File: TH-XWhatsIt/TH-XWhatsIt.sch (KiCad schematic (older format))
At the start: 33 parts, among them J1 COLUMNS, J12 EXPANSION HEADER, J2 ROWS, U1 LM339, U2 MCP4921-EP, U3 74HCT595, U5 74HCT595, U6 LM339, U7 ProMicro, U8 74HCT595

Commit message: Added pads to short reset on bottom
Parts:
- added J13: Conn_01x02, TH-XWhatsIt:PadsToShort, symbol Connector_Generic:Conn_01x02
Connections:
- net GNDA: now also J13.1 (Pin_1)
- net RESET: now reaches U7.22 (RST)
- net RESET: now also J13.2 (Pin_2)
- no-connect marks 5 -> 4
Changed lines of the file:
@@
 $EndComp
 NoConn ~ 9850 2725
-NoConn ~ 9850 2925
 Text GLabel 8450 3225 0    50   Input ~ 0
 ROW1
@@
 ROW7
 Wire Wire Line
-	2000 2075 1775 2075
-Wire Wire Line
 	1625 2075 1625 1475
 Connection ~ 1625 1475
@@
 	1    0    0    -1
 $EndComp
-Connection ~ 1775 2075
-Wire Wire Line
-	1775 2075 1725 2075
 Connection ~ 1725 2075
 Wire Wire Line
@@
 Text Notes 1025 750  0    50   ~ 0
 Either mount just the resistor networks,\nor mount just the individual pulls to BIAS.
+Wire Wire Line
+	1725 2075 2000 2075
+Text GLabel 9850 2925 2    50   UnSpc ~ 0
+RESET
+Text GLabel 5925 6450 2    50   UnSpc ~ 0
+RESET
+$Comp
+L power:GNDD #PWR0104
+U 1 1 5F51A5A9
+P 5925 6550
+F 0 "#PWR0104" H 5925 6300 50  0001 C CNN
+F 1 "GNDD" H 5929 6395 50  0000 C CNN
+F 2 "" H 5925 6550 50  0001 C CNN
+F 3 "" H 5925 6550 50  0001 C CNN
+	1    5925 6550
+	1    0    0    -1
+$EndComp
+$Comp
+L Connector_Generic:Conn_01x02 J13
+U 1 1 5F5276AE
+P 5725 6550
+F 0 "J13" H 5643 6225 50  0000 C CNN
+F 1 "Conn_01x02" H 5643 6316 50  0000 C CNN
+F 2 "TH-XWhatsIt:PadsToShort" H 5725 6550 50  0001 C CNN
+F 3 "~" H 5725 6550 50  0001 C CNN
+	1    5725 6550
+	-1   0    0    1
+$EndComp
 $EndSCHEMATC

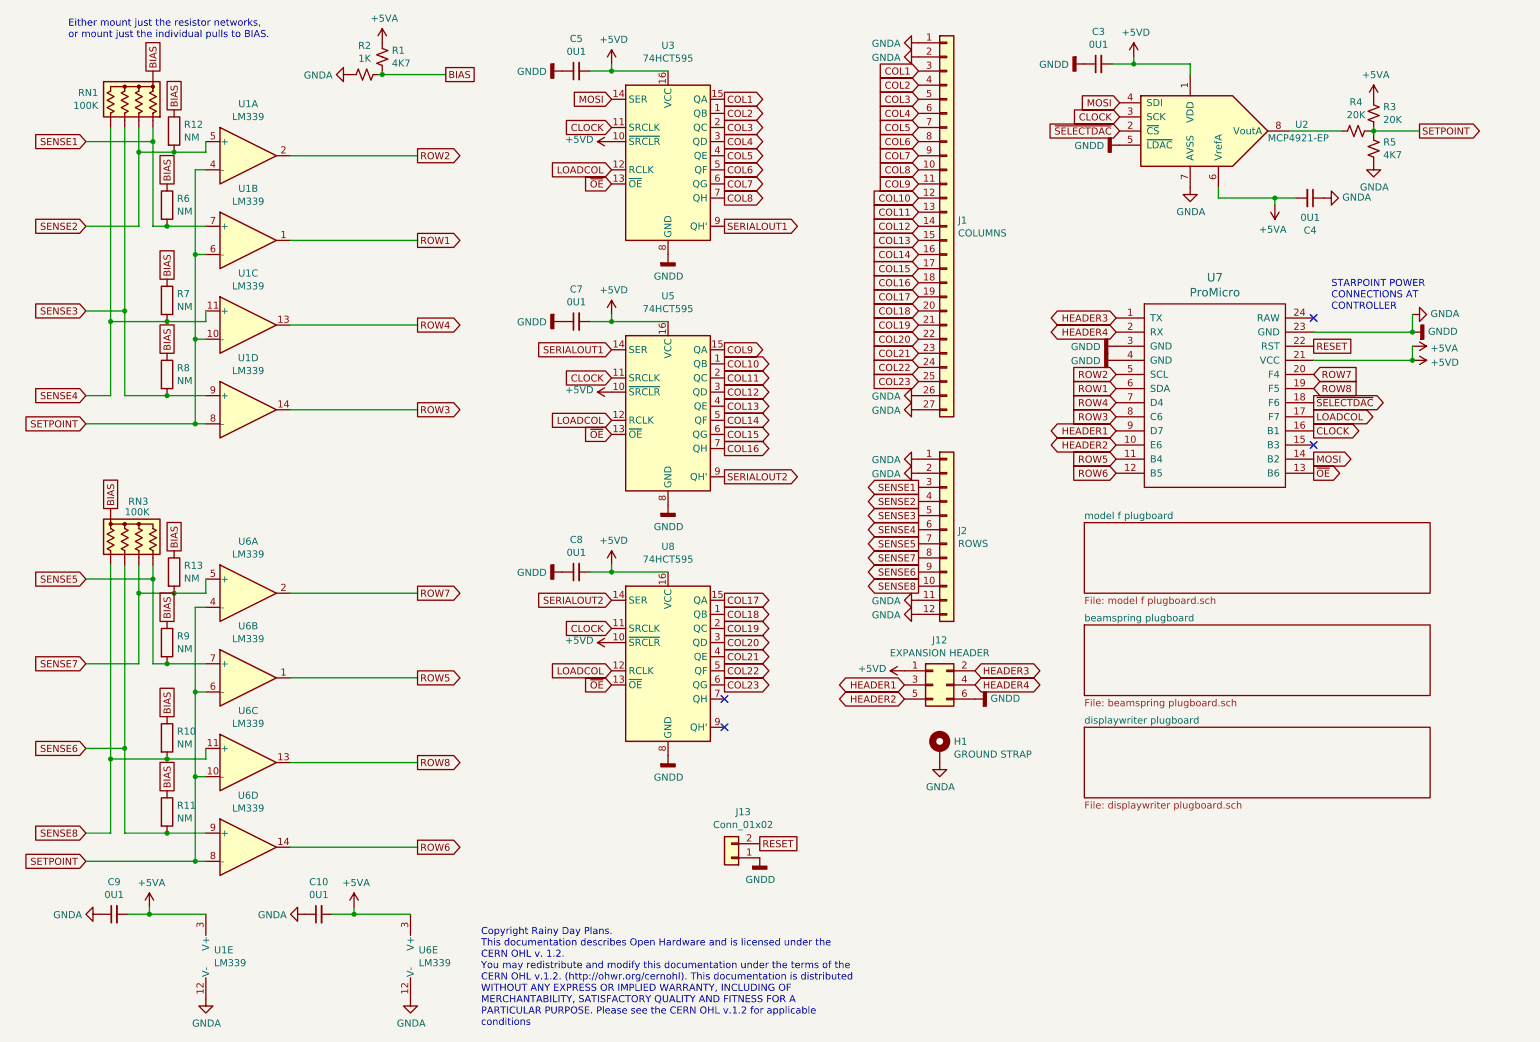
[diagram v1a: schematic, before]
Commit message: Use net tie to enforce star ground on the controller
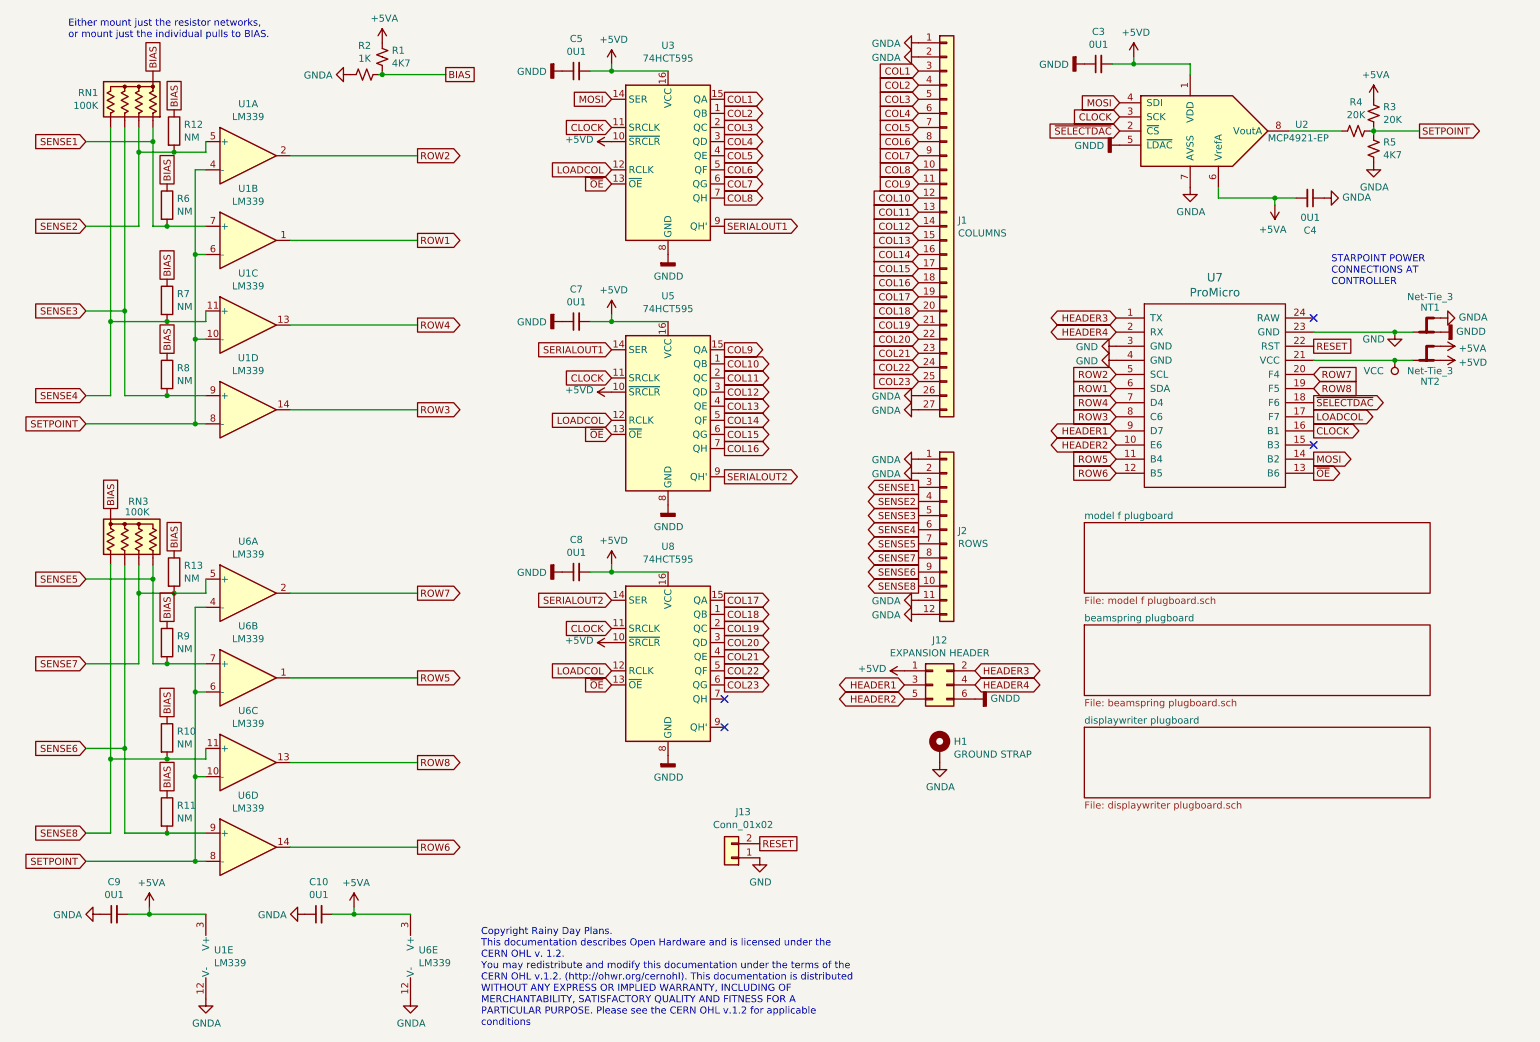
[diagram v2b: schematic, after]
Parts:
- added NT1, NT2: Net-Tie_3, NetTie:NetTie-3_THT_Pad1.0mm, symbol Device:Net-Tie_3
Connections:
- net +5VA: now also NT2.3; no longer C3.2, C5.2, C7.2, C8.2, J12.1 (Pin_1), U2.1 (VDD), U3.10 (~SRCLR), U3.16 (VCC), U5.10 (~SRCLR), U5.16 (VCC), U7.21 (VCC), U8.10 (~SRCLR), U8.16 (VCC)
- net GNDA: now also NT1.3; no longer C3.1, C5.1, C7.1, C8.1, J12.6 (Pin_6), J13.1 (Pin_1), U2.5 (~LDAC~), U3.8 (GND), U5.8 (GND), U7.23 (GND), U7.3 (GND), U7.4 (GND), U8.8 (GND)
- new net +5VD: C3.2, C5.2, C7.2, C8.2, J12.1 (Pin_1), NT2.1, U2.1 (VDD), U3.10 (~SRCLR), U3.16 (VCC), U5.10 (~SRCLR), U5.16 (VCC), U8.10 (~SRCLR), U8.16 (VCC)
- new net GND: J13.1 (Pin_1), NT1.2, U7.23 (GND), U7.3 (GND), U7.4 (GND)
- new net GNDD: C3.1, C5.1, C7.1, C8.1, J12.6 (Pin_6), NT1.1, U2.5 (~LDAC~), U3.8 (GND), U5.8 (GND), U8.8 (GND)
- new net VCC: NT2.2, U7.21 (VCC)
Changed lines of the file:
@@
-$EndComp
-$Comp
-L power:GNDD #PWR0102
-U 1 1 5E8149BA
-P 8450 2925
-F 0 "#PWR0102" H 8450 2675 50  0001 C CNN
-F 1 "GNDD" V 8454 2815 50  0000 R CNN
-F 2 "" H 8450 2925 50  0001 C CNN
-F 3 "" H 8450 2925 50  0001 C CNN
-	1    8450 2925
-	0    1    1    0
 $EndComp
 $Comp
@@
 	1    4875 4475
 	1    0    0    -1
-$EndComp
-$Comp
-L power:+5VD #PWR0110
-U 1 1 5E81915B
-P 10550 3025
-F 0 "#PWR0110" H 10550 2875 50  0001 C CNN
-F 1 "+5VD" V 10565 3153 50  0000 L CNN
-F 2 "" H 10550 3025 50  0001 C CNN
-F 3 "" H 10550 3025 50  0001 C CNN
-	1    10550 3025
-	0    1    1    0
 $EndComp
 $Comp
@@
 $EndComp
 $Comp
-L power:GNDD #PWR0117
-U 1 1 5E82307B
-P 8450 3025
-F 0 "#PWR0117" H 8450 2775 50  0001 C CNN
-F 1 "GNDD" V 8454 2915 50  0000 R CNN
-F 2 "" H 8450 3025 50  0001 C CNN
-F 3 "" H 8450 3025 50  0001 C CNN
-	1    8450 3025
-	0    1    1    0
-$EndComp
-$Comp
-L power:GNDD #PWR0118
-U 1 1 5E823659
-P 10550 2825
-F 0 "#PWR0118" H 10550 2575 50  0001 C CNN
-F 1 "GNDD" V 10554 2715 50  0000 R CNN
-F 2 "" H 10550 2825 50  0001 C CNN
-F 3 "" H 10550 2825 50  0001 C CNN
-	1    10550 2825
-	0    -1   -1   0
-$EndComp
-$Comp
 L power:GNDD #PWR0119
 U 1 1 5E824A24
@@
 	0    1    1    0
 $EndComp
-$Comp
-L power:+5VA #PWR0146
-U 1 1 5E8BFA71
-P 10550 2925
-F 0 "#PWR0146" H 10550 2775 50  0001 C CNN
-F 1 "+5VA" V 10565 3053 50  0000 L CNN
-F 2 "" H 10550 2925 50  0001 C CNN
-F 3 "" H 10550 2925 50  0001 C CNN
-	1    10550 2925
-	0    1    1    0
-$EndComp
-$Comp
-L power:GNDA #PWR0147
-U 1 1 5E8BFD09
-P 10550 2700
-F 0 "#PWR0147" H 10550 2450 50  0001 C CNN
-F 1 "GNDA" V 10555 2572 50  0000 R CNN
-F 2 "" H 10550 2700 50  0001 C CNN
-F 3 "" H 10550 2700 50  0001 C CNN
-	1    10550 2700
-	0    -1   -1   0
-$EndComp
-Wire Wire Line
-	9850 3025 10550 3025
-Wire Wire Line
-	10550 3025 10550 2925
-Connection ~ 10550 3025
-Wire Wire Line
-	10550 2700 10550 2825
-Wire Wire Line
-	10550 2825 9850 2825
-Connection ~ 10550 2825
-Text Notes 9975 2675 0    50   ~ 0
+Wire Wire Line
+	10550 2825 10425 2825
+Text Notes 9975 2500 0    50   ~ 0
 STARPOINT POWER\nCONNECTIONS AT\nCONTROLLER
 $Comp
@@
 RESET
 $Comp
-L power:GNDD #PWR0104
-U 1 1 5F51A5A9
-P 5925 6550
-F 0 "#PWR0104" H 5925 6300 50  0001 C CNN
-F 1 "GNDD" H 5929 6395 50  0000 C CNN
-F 2 "" H 5925 6550 50  0001 C CNN
-F 3 "" H 5925 6550 50  0001 C CNN
-	1    5925 6550
-	1    0    0    -1
-$EndComp
-$Comp
 L Connector_Generic:Conn_01x02 J13
 U 1 1 5F5276AE
@@
 	-1   0    0    1
 $EndComp
+$Comp
+L Device:Net-Tie_3 NT1
+U 1 1 5F549EF2
+P 10650 2825
+F 0 "NT1" H 10625 2650 50  0000 C CNN
+F 1 "Net-Tie_3" H 10625 2575 50  0000 C CNN
+F 2 "NetTie:NetTie-3_THT_Pad1.0mm" H 10650 2825 50  0001 C CNN
+F 3 "~" H 10650 2825 50  0001 C CNN
+	1    10650 2825
+	-1   0    0    1
+$EndComp
+$Comp
+L power:+5VD #PWR0110
+U 1 1 5E81915B
+P 10750 3025
+F 0 "#PWR0110" H 10750 2875 50  0001 C CNN
+F 1 "+5VD" V 10765 3153 50  0000 L CNN
+F 2 "" H 10750 3025 50  0001 C CNN
+F 3 "" H 10750 3025 50  0001 C CNN
+	1    10750 3025
+	0    1    1    0
+$EndComp
+$Comp
+L power:+5VA #PWR0146
+U 1 1 5E8BFA71
+P 10750 2925
+F 0 "#PWR0146" H 10750 2775 50  0001 C CNN
+F 1 "+5VA" V 10765 3053 50  0000 L CNN
+F 2 "" H 10750 2925 50  0001 C CNN
+F 3 "" H 10750 2925 50  0001 C CNN
+	1    10750 2925
+	0    1    1    0
+$EndComp
+$Comp
+L power:GNDD #PWR0118
+U 1 1 5E823659
+P 10750 2825
+F 0 "#PWR0118" H 10750 2575 50  0001 C CNN
+F 1 "GNDD" V 10754 2715 50  0000 R CNN
+F 2 "" H 10750 2825 50  0001 C CNN
+F 3 "" H 10750 2825 50  0001 C CNN
+	1    10750 2825
+	0    -1   -1   0
+$EndComp
+$Comp
+L power:GNDA #PWR0147
+U 1 1 5E8BFD09
+P 10750 2725
+F 0 "#PWR0147" H 10750 2475 50  0001 C CNN
+F 1 "GNDA" V 10755 2597 50  0000 R CNN
+F 2 "" H 10750 2725 50  0001 C CNN
+F 3 "" H 10750 2725 50  0001 C CNN
+	1    10750 2725
+	0    -1   -1   0
+$EndComp
+$Comp
+L Device:Net-Tie_3 NT2
+U 1 1 5F54AB7C
+P 10650 3025
+F 0 "NT2" H 10625 3175 50  0000 C CNN
+F 1 "Net-Tie_3" H 10625 3100 50  0000 C CNN
+F 2 "NetTie:NetTie-3_THT_Pad1.0mm" H 10650 3025 50  0001 C CNN
+F 3 "~" H 10650 3025 50  0001 C CNN
+	1    10650 3025
+	-1   0    0    1
+$EndComp
+$Comp
+L power:GND #PWR0102
+U 1 1 5F57039E
+P 10425 2825
+F 0 "#PWR0102" H 10425 2575 50  0001 C CNN
+F 1 "GND" H 10275 2775 50  0000 C CNN
+F 2 "" H 10425 2825 50  0001 C CNN
+F 3 "" H 10425 2825 50  0001 C CNN
+	1    10425 2825
+	1    0    0    -1
+$EndComp
+$Comp
+L power:GND #PWR0104
+U 1 1 5F573194
+P 5925 6550
+F 0 "#PWR0104" H 5925 6300 50  0001 C CNN
+F 1 "GND" H 5930 6377 50  0000 C CNN
+F 2 "" H 5925 6550 50  0001 C CNN
+F 3 "" H 5925 6550 50  0001 C CNN
+	1    5925 6550
+	1    0    0    -1
+$EndComp
+$Comp
+L power:GND #PWR0105
+U 1 1 5F579EDB
+P 8450 2925
+F 0 "#PWR0105" H 8450 2675 50  0001 C CNN
+F 1 "GND" V 8455 2797 50  0000 R CNN
+F 2 "" H 8450 2925 50  0001 C CNN
+F 3 "" H 8450 2925 50  0001 C CNN
+	1    8450 2925
+	0    1    1    0
+$EndComp
+$Comp
+L power:GND #PWR0112
+U 1 1 5F57A4BB
+P 8450 3025
+F 0 "#PWR0112" H 8450 2775 50  0001 C CNN
+F 1 "GND" V 8455 2897 50  0000 R CNN
+F 2 "" H 8450 3025 50  0001 C CNN
+F 3 "" H 8450 3025 50  0001 C CNN
+	1    8450 3025
+	0    1    1    0
+$EndComp
+Connection ~ 10425 2825
+Wire Wire Line
+	10425 2825 9850 2825
+Wire Wire Line
+	9850 3025 10425 3025
+$Comp
+L power:VCC #PWR?
+U 1 1 5F585D6B
+P 10425 3025
+F 0 "#PWR?" H 10425 2875 50  0001 C CNN
+F 1 "VCC" H 10575 3100 50  0000 C CNN
+F 2 "" H 10425 3025 50  0001 C CNN
+F 3 "" H 10425 3025 50  0001 C CNN
+	1    10425 3025
+	-1   0    0    1
+$EndComp
+Connection ~ 10425 3025
+Wire Wire Line
+	10425 3025 10550 3025
 $EndSCHEMATC

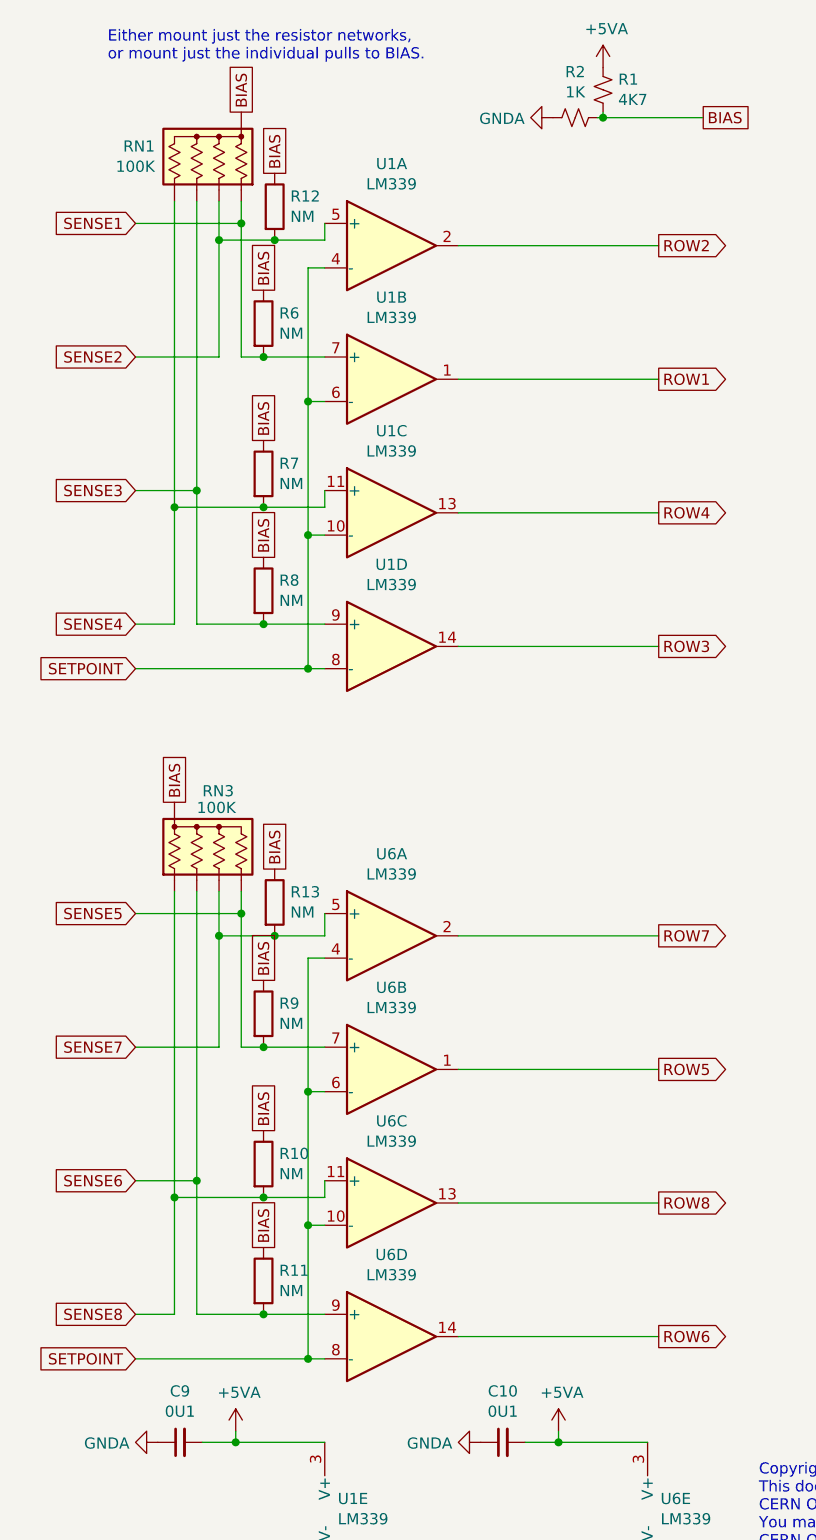
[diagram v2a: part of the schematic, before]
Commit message: I'm just after realizing that this PCB was using the style where the component values are on silkscreen but not the RefDes. Making my changes match this style.
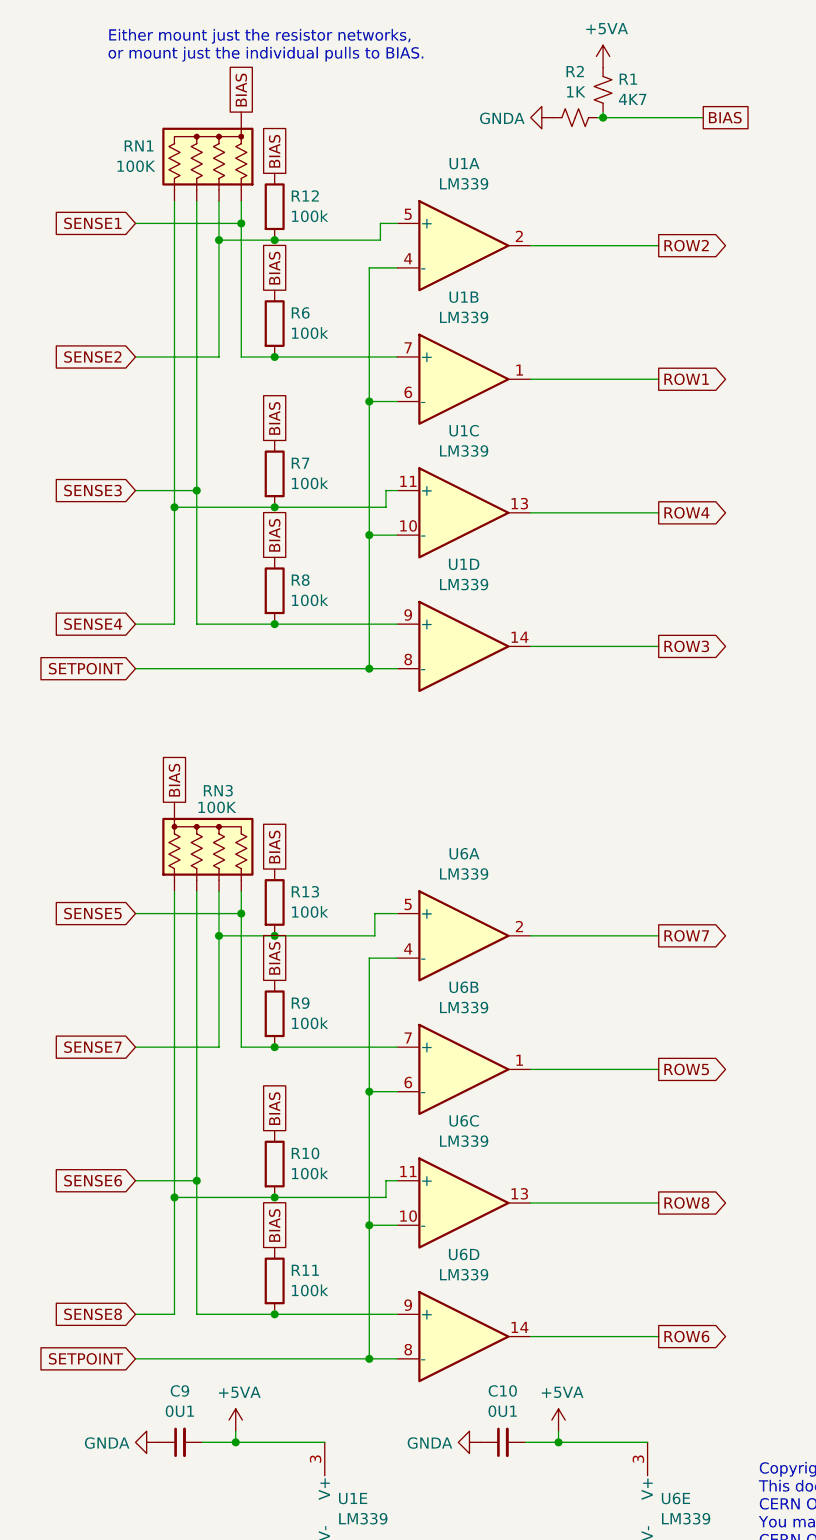
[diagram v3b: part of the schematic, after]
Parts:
- R10, R11, R12, R13, R6, R7, R8, R9: value NM -> 100k
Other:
- moved on the sheet: R10, R11, R6, R7, R8, R9, U1A, U1B, U1C, U1D, U6A, U6B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

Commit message: Made net ties thicker
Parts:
- NT1, NT2: footprint NetTie:NetTie-3_THT_Pad1.0mm -> TH-XWhatsIt:NetTie-3_THT_Pad1.0mm_mod_thicker
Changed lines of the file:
@@
 F 0 "NT1" H 10625 2650 50  0000 C CNN
 F 1 "Net-Tie_3" H 10625 2575 50  0000 C CNN
-F 2 "NetTie:NetTie-3_THT_Pad1.0mm" H 10650 2825 50  0001 C CNN
+F 2 "TH-XWhatsIt:NetTie-3_THT_Pad1.0mm_mod_thicker" H 10650 2825 50  0001 C CNN
 F 3 "~" H 10650 2825 50  0001 C CNN
 	1    10650 2825
@@
 F 0 "NT2" H 10625 3175 50  0000 C CNN
 F 1 "Net-Tie_3" H 10625 3100 50  0000 C CNN
-F 2 "NetTie:NetTie-3_THT_Pad1.0mm" H 10650 3025 50  0001 C CNN
+F 2 "TH-XWhatsIt:NetTie-3_THT_Pad1.0mm_mod_thicker" H 10650 3025 50  0001 C CNN
 F 3 "~" H 10650 3025 50  0001 C CNN
 	1    10650 3025
